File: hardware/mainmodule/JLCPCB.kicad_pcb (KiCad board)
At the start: 2 copper layers, 83.8 x 61 mm, 74 parts, among them J1 USB+, J10 Conn_01x04, J2 To LED_MOD_0, J3 To EXT_MOD_1, J4 V24_IN, J5 Temp, J6 Presence, J7 Neo, J8 AUX, J9 Conn_01x04, Q1 Si3456DDV, Q2 Si3456DDV, Q3 Si3456DDV, Q4 Si3456DDV, Q5 Si3456DDV, Q6 Si3456DDV, SW1 SW_Push, SW2 SW_Push, U1 ESP32-C6-WROOM-1, U2 VEML6040A3OG, U3 74HCT244, U4 DS18B20U, U5 MC34063AD

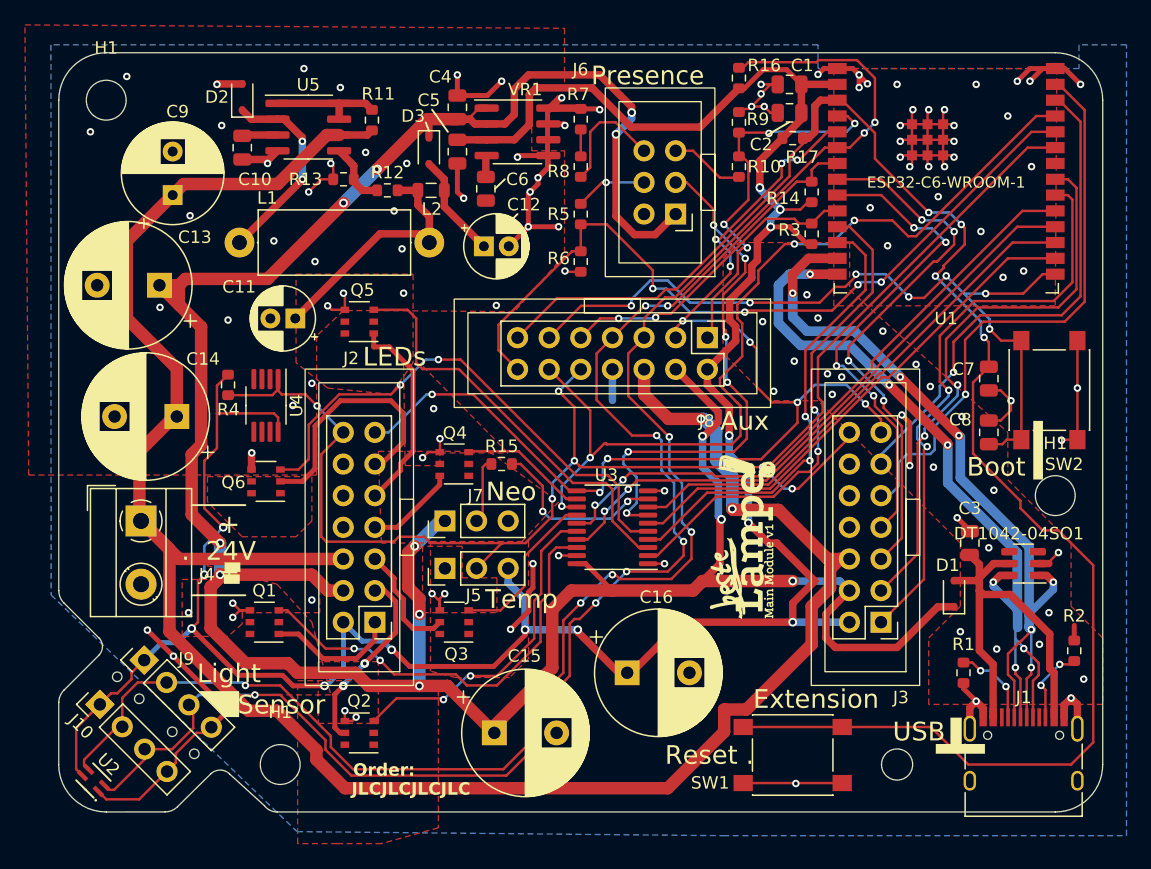
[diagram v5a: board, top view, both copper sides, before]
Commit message: Update version in Silkscreen. Many small optimizations.
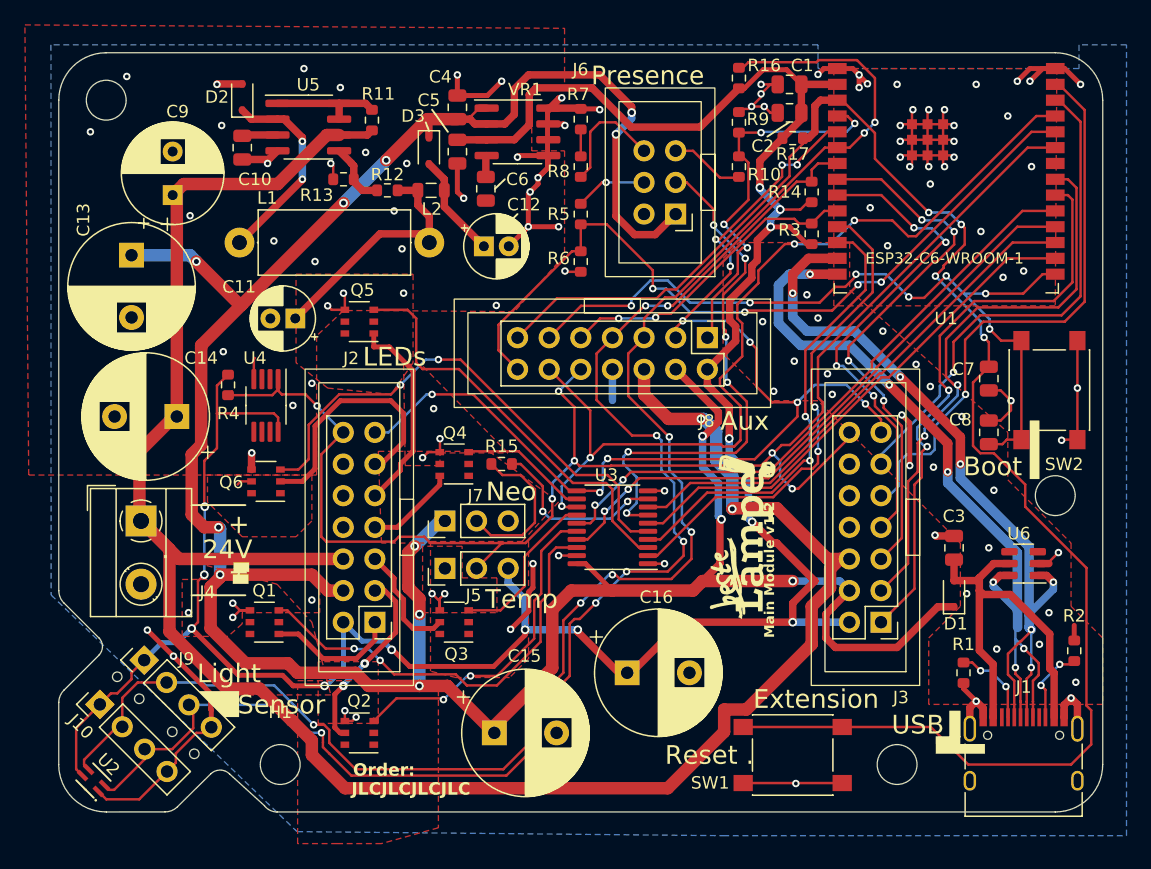
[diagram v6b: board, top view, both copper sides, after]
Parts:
- H3: footprint MountingHole:MountingHole_2.5mm -> MountingHole:MountingHole_3.2mm_M3
- U6: renamed from DT1042-04SO1; value ~ -> DT1042-04SO1
- moved C13 3.29 mm to (70.6, 64.5), turned to -90 degrees
- moved C3 1.33 mm to (136.7, 88.0)
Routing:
- net Net-(J7-Pin_2): track 5.33 -> 12.6 mm
- net +24V: track 180.2 -> 177.1 mm
- net +5V: track 229.9 -> 231.9 mm, vias 12 -> 13
- net GND: track 189.6 -> 188.0 mm, vias 118 -> 116
- net +3.3V: track 213.5 -> 212.0 mm
- net /L0.6: track 20.3 -> 21.6 mm
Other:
- board text added: "Main Module v1.2"
- board text removed: "Main Module v1"
